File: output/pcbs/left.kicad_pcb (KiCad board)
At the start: 2 copper layers, 123.1 x 95.2 mm, 40 parts

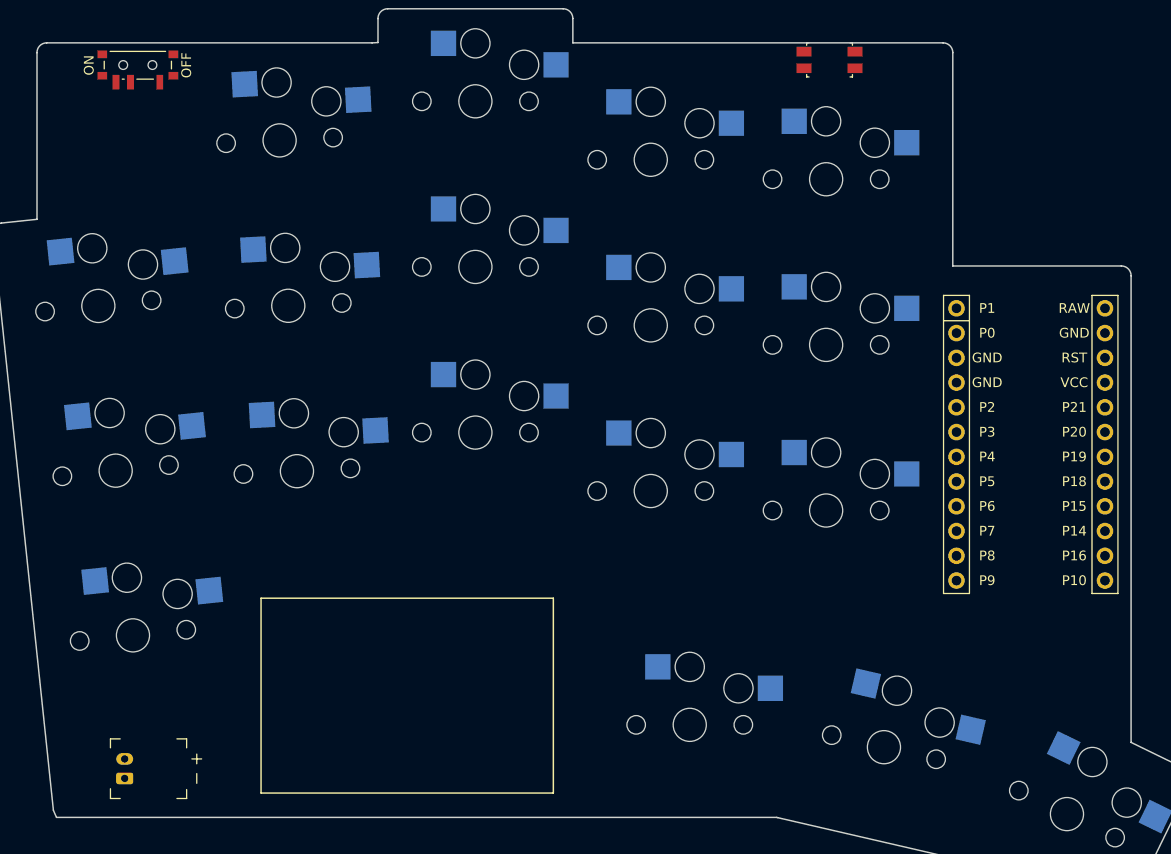
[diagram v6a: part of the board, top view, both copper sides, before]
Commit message: Add mounting holes
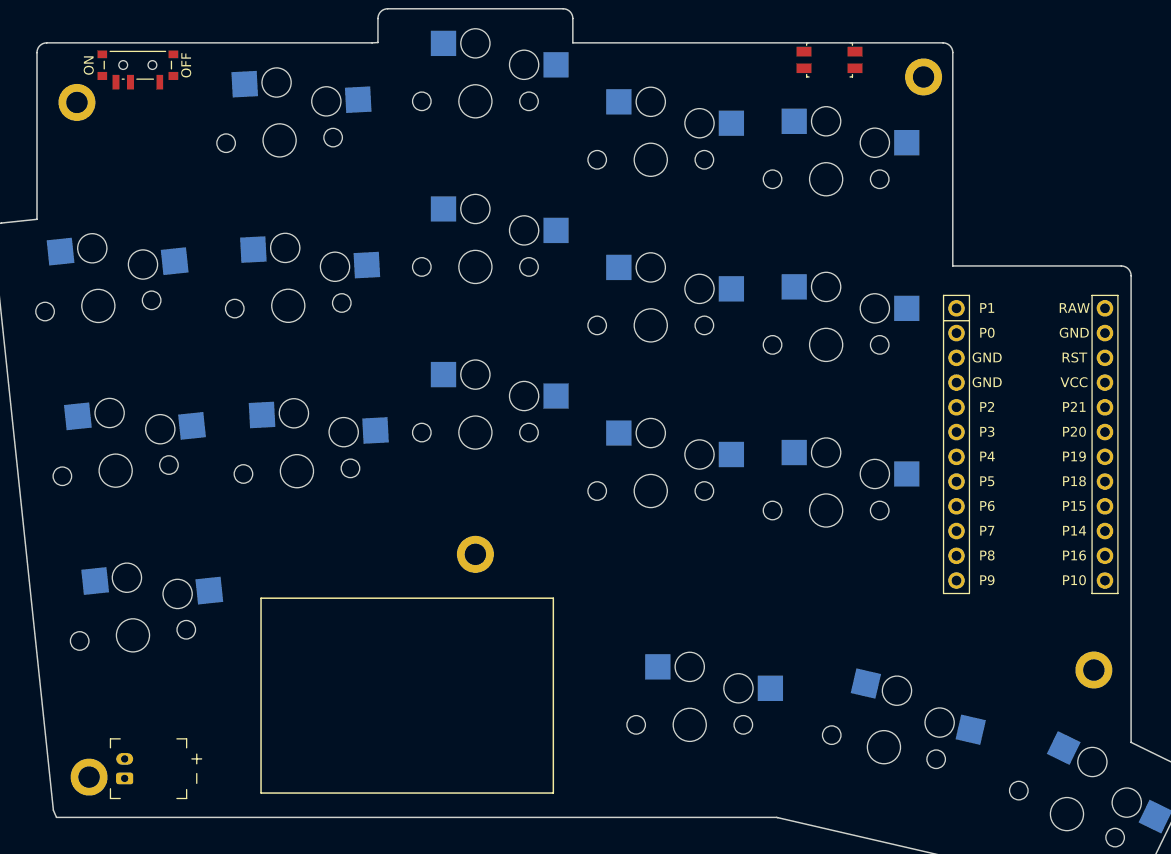
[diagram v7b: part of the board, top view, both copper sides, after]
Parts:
- added H1: , ceoloide:mounting_hole_plated, F.Cu at (-5.75, -54.7)
- added H2: , ceoloide:mounting_hole_plated, F.Cu at (81.1, -57.3)
- added H3: , ceoloide:mounting_hole_plated, F.Cu at (-4.50, 14.6)
- added H4: , ceoloide:mounting_hole_plated, F.Cu at (35.1, -8.32)
- added H5: , ceoloide:mounting_hole_plated, F.Cu at (98.6, 3.56)
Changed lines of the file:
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@@
         (pad "2" thru_hole oval (at 1 0 90) (size 1.2 1.75) (drill 0.75) (layers "*.Cu" "*.Mask") (net 124 "BAT_P"))
     )
+  (footprint "ceoloide:mounting_hole_plated"
+    (layer "F.Cu")
+    (at -5.7490655 -54.698704199999995 6)
+    (property "Reference" "H1"
+      (at 0 3 6)
+      (layer "F.SilkS")
+      hide
+      (effects (font (size 1 1) (thickness 0.15)))
+    )
+    (pad "" thru_hole circle (at 0 0 6) (size 3.8000000000000003 3.8000000000000003) (drill 2.2) (layers "*.Cu" "*.Mask"))
+    (fp_circle (center 0 0) (end -2.1500000000000004 0) (layer "F.CrtYd") (stroke (width 0.05) (type solid)) (fill none))
+    (fp_circle (center 0 0) (end -2.1500000000000004 0) (layer "B.CrtYd") (stroke (width 0.05) (type solid)) (fill none))
+  )
+  (footprint "ceoloide:mounting_hole_plated"
+    (layer "F.Cu")
+    (at 81.1483666 -57.315708900000004 0)
+    (property "Reference" "H2"
+      (at 0 3 0)
+      (layer "F.SilkS")
+      hide
+      (effects (font (size 1 1) (thickness 0.15)))
+    )
+    (pad "" thru_hole circle (at 0 0 0) (size 3.8000000000000003 3.8000000000000003) (drill 2.2) (layers "*.Cu" "*.Mask"))
+    (fp_circle (center 0 0) (end -2.1500000000000004 0) (layer "F.CrtYd") (stroke (width 0.05) (type solid)) (fill none))
+    (fp_circle (center 0 0) (end -2.1500000000000004 0) (layer "B.CrtYd") (stroke (width 0.05) (type solid)) (fill none))
+  )
+  (footprint "ceoloide:mounting_hole_plated"
+    (layer "F.Cu")
+    (at -4.5037329 14.5504773 6)
+    (property "Reference" "H3"
+      (at 0 3 6)
+      (layer "F.SilkS")
+      hide
+      (effects (font (size 1 1) (thickness 0.15)))
+    )
+    (pad "" thru_hole circle (at 0 0 6) (size 3.8000000000000003 3.8000000000000003) (drill 2.2) (layers "*.Cu" "*.Mask"))
+    (fp_circle (center 0 0) (end -2.1500000000000004 0) (layer "F.CrtYd") (stroke (width 0.05) (type solid)) (fill none))
+    (fp_circle (center 0 0) (end -2.1500000000000004 0) (layer "B.CrtYd") (stroke (width 0.05) (type solid)) (fill none))
+  )
+  (footprint "ceoloide:mounting_hole_plated"
+    (layer "F.Cu")
+    (at 35.1483667 -8.3157088 0)
+    (property "Reference" "H4"
+      (at 0 3 0)
+      (layer "F.SilkS")
+      hide
+      (effects (font (size 1 1) (thickness 0.15)))
+    )
+    (pad "" thru_hole circle (at 0 0 0) (size 3.8000000000000003 3.8000000000000003) (drill 2.2) (layers "*.Cu" "*.Mask"))
+    (fp_circle (center 0 0) (end -2.1500000000000004 0) (layer "F.CrtYd") (stroke (width 0.05) (type solid)) (fill none))
+    (fp_circle (center 0 0) (end -2.1500000000000004 0) (layer "B.CrtYd") (stroke (width 0.05) (type solid)) (fill none))
+  )
+  (footprint "ceoloide:mounting_hole_plated"
+    (layer "F.Cu")
+    (at 98.6292952 3.5592457000000017 -26)
+    (property "Reference" "H5"
+      (at 0 3 -26)
+      (layer "F.SilkS")
+      hide
+      (effects (font (size 1 1) (thickness 0.15)))
+    )
+    (pad "" thru_hole circle (at 0 0 -26) (size 3.8000000000000003 3.8000000000000003) (drill 2.2) (layers "*.Cu" "*.Mask"))
+    (fp_circle (center 0 0) (end -2.1500000000000004 0) (layer "F.CrtYd") (stroke (width 0.05) (type solid)) (fill none))
+    (fp_circle (center 0 0) (end -2.1500000000000004 0) (layer "B.CrtYd") (stroke (width 0.05) (type solid)) (fill none))
+  )
   (gr_line (start 45.148366599999996 -60.815708799999996) (end 45.1483667 -63.315708799999996) (layer Edge.Cuts) (stroke (width 0.15) (type default)))
 (gr_arc (start 45.1483667 -63.315708799999996) (mid 44.855473499999995 -64.0228156) (end 44.1483667 -64.3157088) (layer Edge.Cuts) (stroke (width 0.15) (type default)))

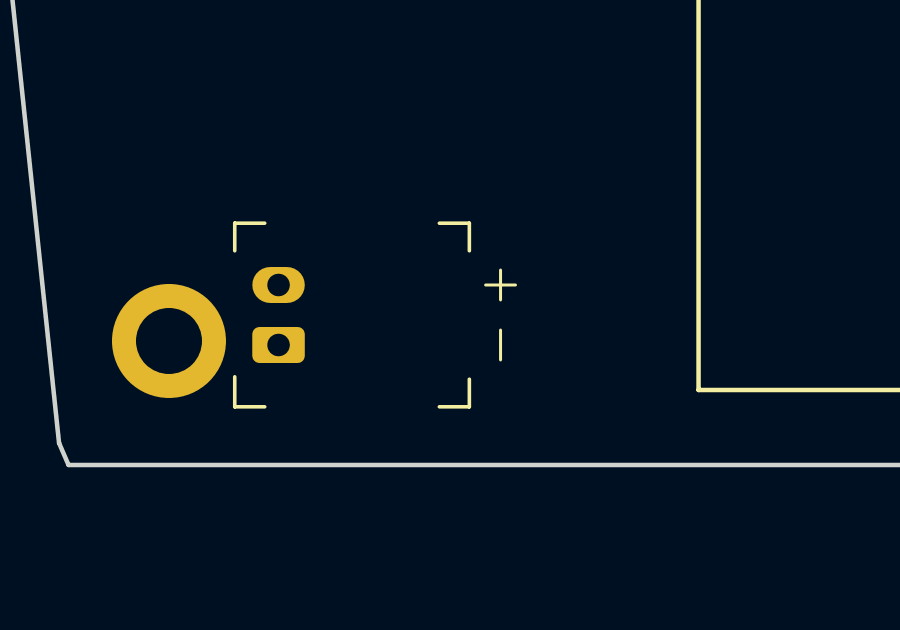
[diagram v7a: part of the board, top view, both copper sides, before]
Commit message: Shift JST
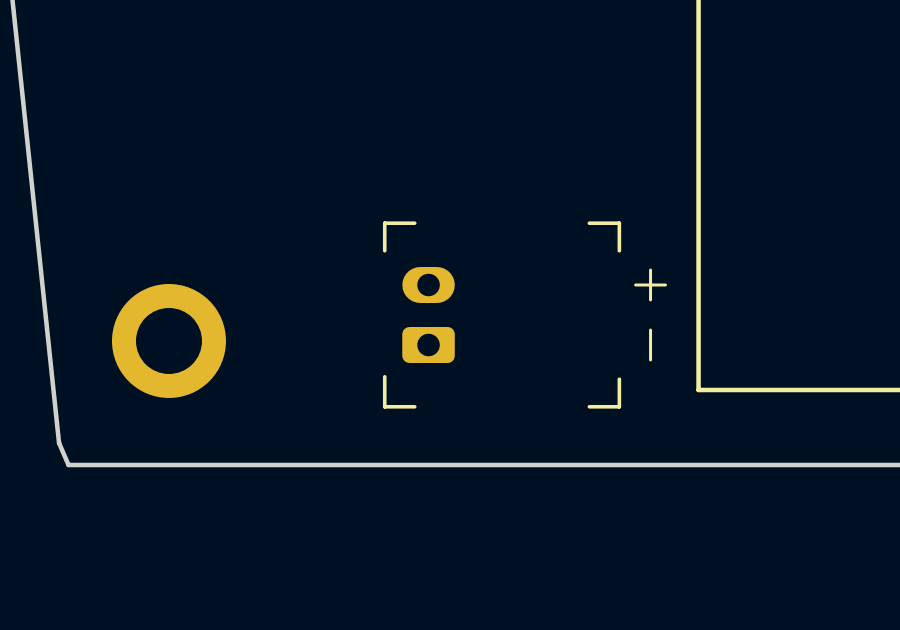
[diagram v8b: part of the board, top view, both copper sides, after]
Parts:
- moved JST1 5.00 mm to (4.15, 13.7)
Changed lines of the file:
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@@
     (footprint "ceoloide:battery_connector_jst_ph_2"
         (layer "F.Cu")
-        (at -0.8516334000000043 13.6842912 90)
+        (at 4.148366599999996 13.6842912 90)
         (property "Reference" "JST1"
             (at 0 4.8 90)
